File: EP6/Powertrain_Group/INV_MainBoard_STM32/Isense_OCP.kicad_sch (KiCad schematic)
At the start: 18 parts, among them J13 motorTemp, J5 current_DC, J6 to PhaseIsense, U15 LM2903

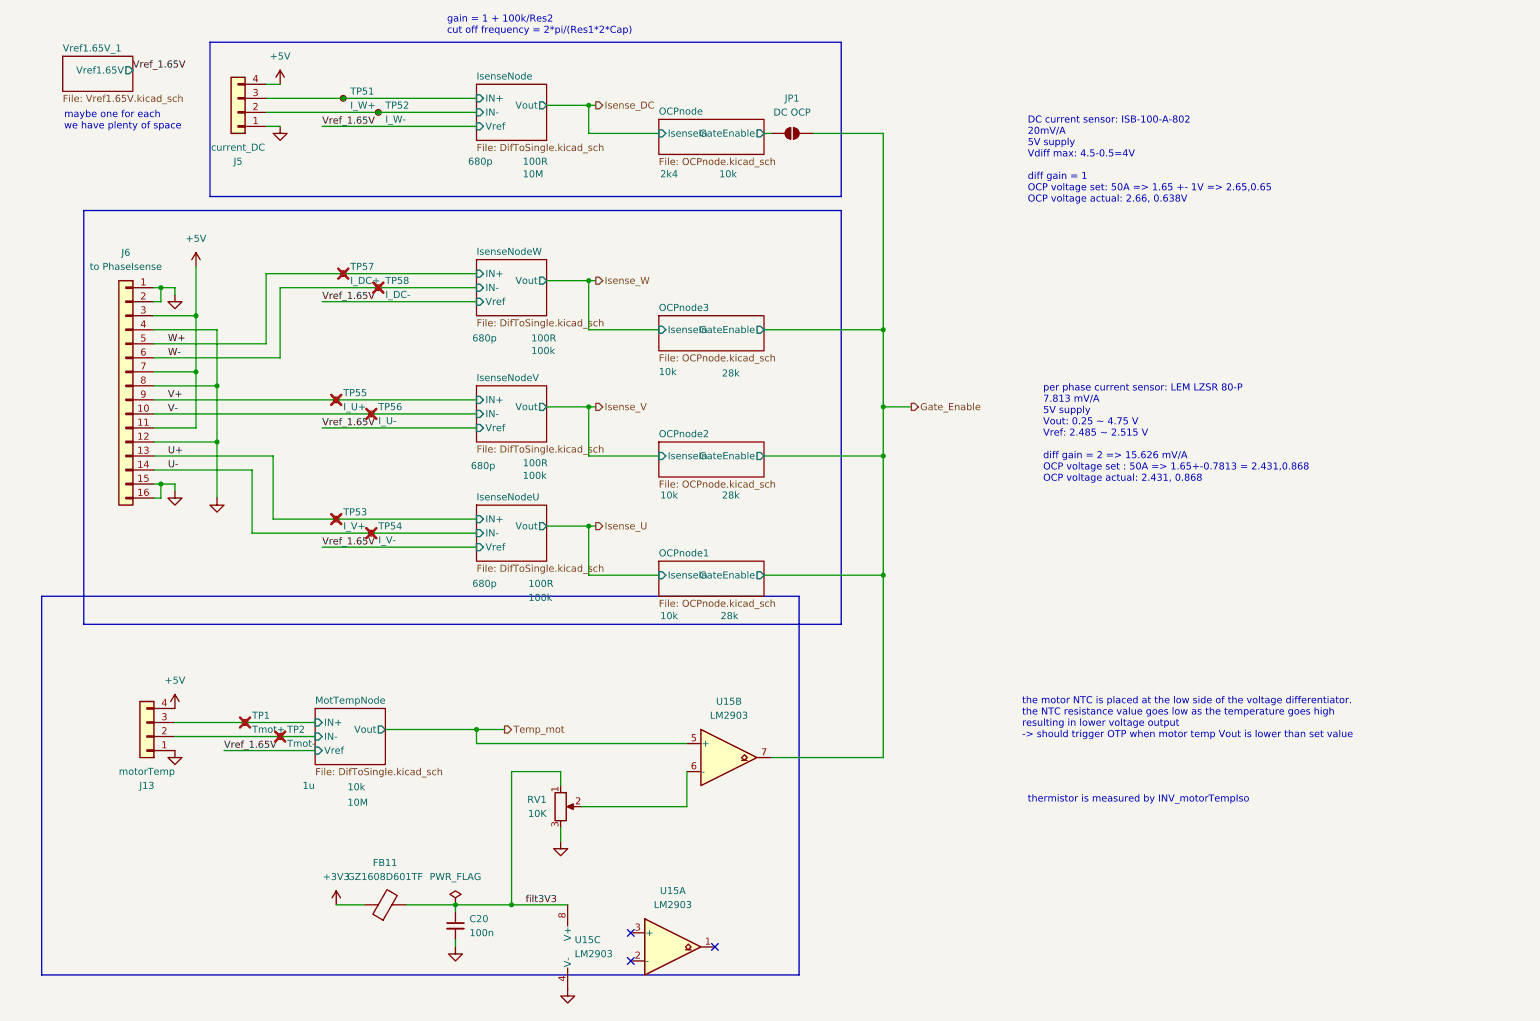
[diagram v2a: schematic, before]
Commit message: update INV_MainBoard_STM32 to V2.1
update for JLCPCB, include change in 1.65 Vref and some name change for easier JLCPCBA BOM selection
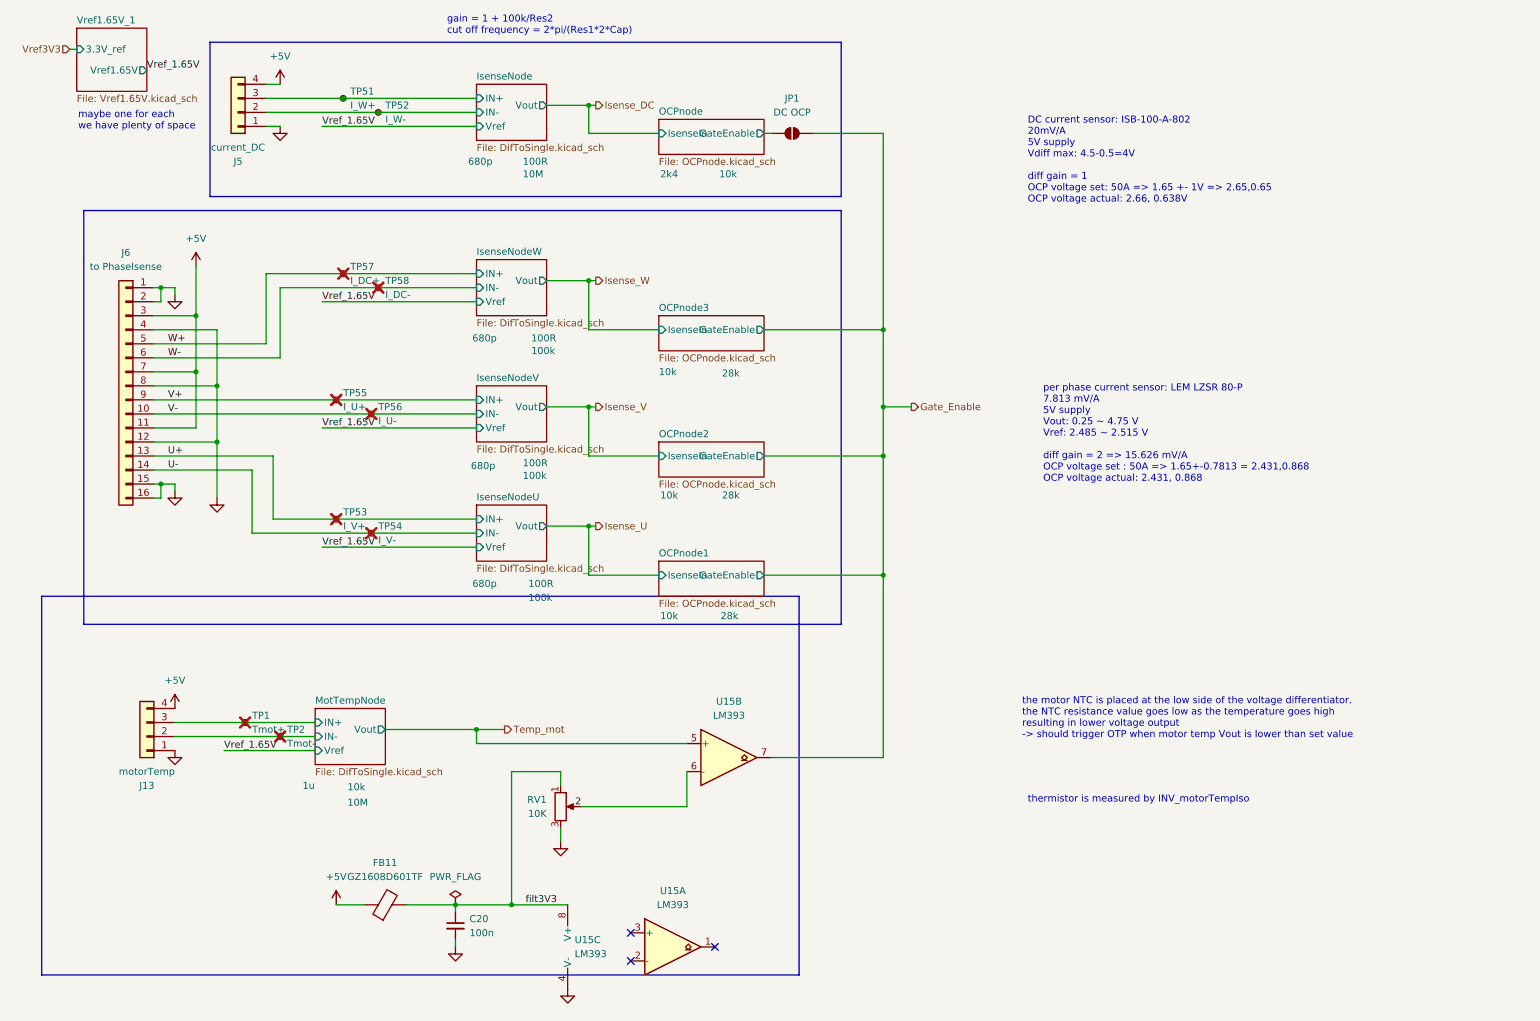
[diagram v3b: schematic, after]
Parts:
- U15: value LM2903 -> LM393; symbol Comparator:LM2903 -> Comparator:LM393
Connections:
- net +3V3 is gone; now on net +5V: FB11.1
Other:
- sheet Vref1.65V_1 ports: added 3.3V_ref; removed none
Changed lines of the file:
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@@
 	(title_block
 		(title "INV_MainBoard_STM32")
-		(rev "2.0")
+		(date "2025-02-28")
+		(rev "2.1")
 		(company "NTURacing Team")
 		(comment 1 "郭哲明 Jack Kuo")
@@
 	(wire
 		(pts
+			(xy 21.59 21.59) (xy 22.86 21.59)
+		)
+		(stroke
+			(width 0)
+			(type default)
+		)
+	)
+	(wire
+		(pts
 			(xy 156.21 36.83) (xy 168.91 36.83)
 		)
@@
 	(text "maybe one for each\nwe have plenty of space "
 		(exclude_from_sim no)
-		(at 20.574 36.322 0)
+		(at 23.114 36.322 0)
 		(effects
 			(font
@@
 	)
 	(label "Vref_1.65V"
-		(at 33.02 25.4 0)
+		(at 35.56 25.4 0)
 		(effects
 			(font
@@
 		)
 	)
+	(hierarchical_label "Vref3V3"
+		(shape input)
+		(at 21.59 21.59 180)
+		(effects
+			(font
+				(size 1.27 1.27)
+			)
+			(justify right)
+		)
+	)
 	(hierarchical_label "Isense_V"
 		(shape output)
@@
 	)
 	(symbol
-		(lib_id "Comparator:LM2903")
+		(lib_id "Comparator:LM393")
 		(at 140.97 149.86 0)
 		(unit 2)
@@
 			)
 		)
-		(property "Value" "LM2903"
+		(property "Value" "LM393"
 			(at 140.97 142.24 0)
 			(effects
@@
 			)
 		)
-		(property "Description" "Low-Power, Low-Offset Voltage, Dual Comparators, DIP-8/SOIC-8/SOP-8/TSSOP-8/VSSOP-8"
+		(property "Description" "Low-Power, Low-Offset Voltage, Dual Comparators, DIP-8/SOIC-8/TO-99-8"
 			(at 140.97 149.86 0)
 			(effects
@@
 	)
 	(symbol
-		(lib_id "power:+3V3")
-		(at 69.85 176.53 0)
-		(unit 1)
-		(exclude_from_sim no)
-		(in_bom yes)
-		(on_board yes)
-		(dnp no)
-		(fields_autoplaced yes)
-		(property "Reference" "#PWR093"
-			(at 69.85 180.34 0)
-			(effects
-				(font
-					(size 1.27 1.27)
-				)
-				(hide yes)
-			)
-		)
-		(property "Value" "+3V3"
-			(at 69.85 171.45 0)
-			(effects
-				(font
-					(size 1.27 1.27)
-				)
-			)
-		)
-		(property "Footprint" ""
-			(at 69.85 176.53 0)
-			(effects
-				(font
-					(size 1.27 1.27)
-				)
-				(hide yes)
-			)
-		)
-		(property "Datasheet" ""
-			(at 69.85 176.53 0)
-			(effects
-				(font
-					(size 1.27 1.27)
-				)
-				(hide yes)
-			)
-		)
-		(property "Description" "Power symbol creates a global label with name \"+3V3\""
-			(at 69.85 176.53 0)
-			(effects
-				(font
-					(size 1.27 1.27)
-				)
-				(hide yes)
-			)
-		)
-		(pin "1"
-		)
-		(instances
-			(project ""
-				(path "/963ad98e-e494-4953-a7e0-8b20a365a35d/a8cbfb17-6eb3-4a23-8b1d-6aae5b32a7fb"
-					(reference "#PWR093")
-					(unit 1)
-				)
-			)
-		)
-	)
-	(symbol
 		(lib_id "Jumper:SolderJumper_2_Open")
 		(at 152.4 36.83 0)
@@
 	)
 	(symbol
-		(lib_id "Comparator:LM2903")
+		(lib_id "Comparator:LM393")
 		(at 130.81 184.15 0)
 		(unit 1)
@@
 			)
 		)
-		(property "Value" "LM2903"
+		(property "Value" "LM393"
 			(at 130.81 176.53 0)
 			(effects
@@
 			)
 		)
-		(property "Description" "Low-Power, Low-Offset Voltage, Dual Comparators, DIP-8/SOIC-8/SOP-8/TSSOP-8/VSSOP-8"
+		(property "Description" "Low-Power, Low-Offset Voltage, Dual Comparators, DIP-8/SOIC-8/TO-99-8"
 			(at 130.81 184.15 0)
 			(effects
@@
 	)
 	(symbol
+		(lib_id "power:+5V")
+		(at 69.85 176.53 0)
+		(unit 1)
+		(exclude_from_sim no)
+		(in_bom yes)
+		(on_board yes)
+		(dnp no)
+		(fields_autoplaced yes)
+		(property "Reference" "#PWR093"
+			(at 69.85 180.34 0)
+			(effects
+				(font
+					(size 1.27 1.27)
+				)
+				(hide yes)
+			)
+		)
+		(property "Value" "+5V"
+			(at 69.85 171.45 0)
+			(effects
+				(font
+					(size 1.27 1.27)
+				)
+			)
+		)
+		(property "Footprint" ""
+			(at 69.85 176.53 0)
+			(effects
+				(font
+					(size 1.27 1.27)
+				)
+				(hide yes)
+			)
+		)
+		(property "Datasheet" ""
+			(at 69.85 176.53 0)
+			(effects
+				(font
+					(size 1.27 1.27)
+				)
+				(hide yes)
+			)
+		)
+		(property "Description" "Power symbol creates a global label with name \"+5V\""
+			(at 69.85 176.53 0)
+			(effects
+				(font
+					(size 1.27 1.27)
+				)
+				(hide yes)
+			)
+		)
+		(pin "1"
+		)
+		(instances
+			(project "INV_MainBoard_STM32"
+				(path "/963ad98e-e494-4953-a7e0-8b20a365a35d/a8cbfb17-6eb3-4a23-8b1d-6aae5b32a7fb"
+					(reference "#PWR093")
+					(unit 1)
+				)
+			)
+		)
+	)
+	(symbol
 		(lib_id "power:GND")
 		(at 40.64 101.6 0)
@@
 	)
 	(symbol
-		(lib_id "Comparator:LM2903")
+		(lib_id "Comparator:LM393")
 		(at 114.3 184.15 0)
 		(unit 3)
@@
 			)
 		)
-		(property "Value" "LM2903"
+		(property "Value" "LM393"
 			(at 113.03 185.42 0)
 			(effects
@@
 			)
 		)
-		(property "Description" "Low-Power, Low-Offset Voltage, Dual Comparators, DIP-8/SOIC-8/SOP-8/TSSOP-8/VSSOP-8"
+		(property "Description" "Low-Power, Low-Offset Voltage, Dual Comparators, DIP-8/SOIC-8/TO-99-8"
 			(at 114.3 184.15 0)
 			(effects
@@
 	)
 	(sheet
-		(at 20.32 22.86)
-		(size 12.7 6.35)
+		(at 22.86 17.78)
+		(size 12.7 11.43)
 		(fields_autoplaced yes)
 		(stroke
@@
 		)
 		(property "Sheetname" "Vref1.65V_1"
-			(at 20.32 22.1484 0)
+			(at 22.86 17.0684 0)
 			(effects
 				(font
@@
 		)
 		(property "Sheetfile" "Vref1.65V.kicad_sch"
-			(at 20.32 29.7946 0)
+			(at 22.86 29.7946 0)
 			(effects
 				(font
@@
 		)
 		(pin "Vref1.65V" output
-			(at 33.02 25.4 0)
+			(at 35.56 25.4 0)
 			(effects
 				(font
@@
 			)
 		)
+		(pin "3.3V_ref" input
+			(at 22.86 21.59 180)
+			(effects
+				(font
+					(size 1.27 1.27)
+				)
+				(justify left)
+			)
+		)

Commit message: update INV_MainBoard_STM32 to V3.0
PCB: INV_MainBoard_STM32 V3.0
V3.0 remove low volte trig
     add RC filt for OCP, OTP
     dedicated OTP, OCP pull down gate enable
     pending: fault hardware OTP/OCP latch
     pending: add QSPI DRAM
     use JST PH
     exterinal pull up for flt, ready
     fix CAN1, 2 label on board
     use 1k, 2k for encoder divider
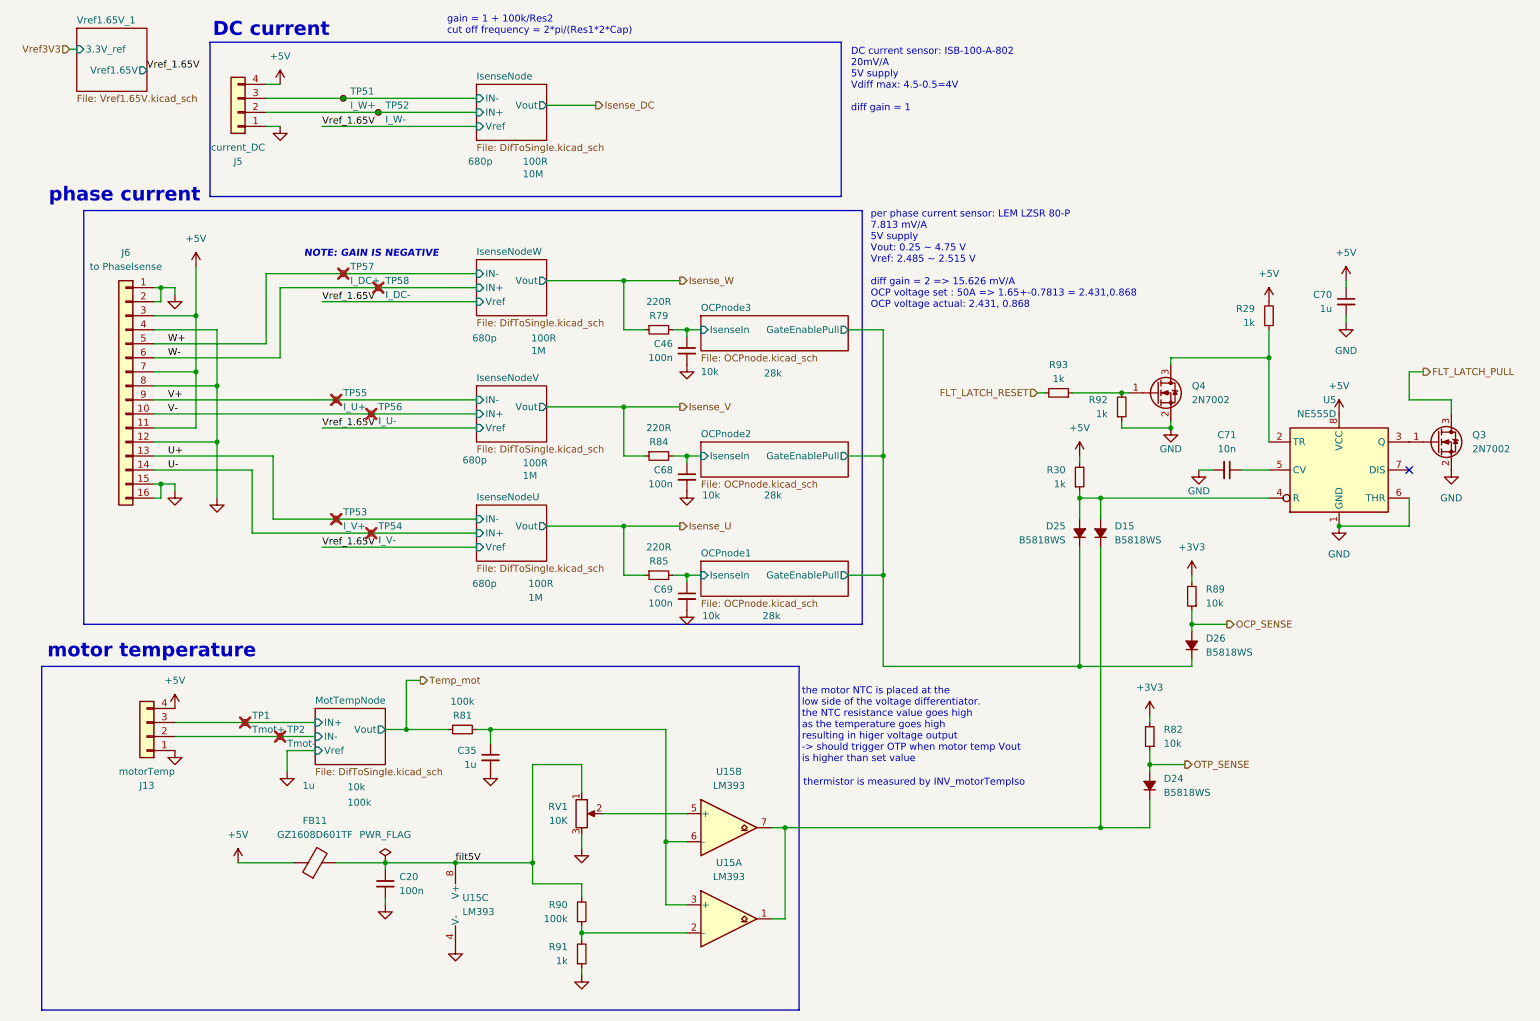
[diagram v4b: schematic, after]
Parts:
- removed JP1: DC OCP, Jumper:SolderJumper-2_P1.3mm_Open_RoundedPad1.0x1.5mm, symbol Jumper:SolderJumper_2_Open
- added C35, C70: 1u, Capacitor_SMD:C_0402_1005Metric, symbol Device:C_Small
- added C46, C68, C69: 100n, Capacitor_SMD:C_0402_1005Metric, symbol Device:C_Small
- added C71: 10n, Capacitor_SMD:C_0402_1005Metric, symbol Device:C_Small
- added D15, D24, D25, D26: B5818WS, Diode_SMD:D_SOD-323, symbol Device:D_Small_Filled
- added Q3, Q4: 2N7002, Package_TO_SOT_SMD:SOT-23, symbol Transistor_FET:2N7002
- added R29, R30, R91, R92, R93: 1k, Resistor_SMD:R_0402_1005Metric, symbol Device:R_Small
- added R79, R84, R85: 220R, Resistor_SMD:R_0402_1005Metric, symbol Device:R_Small
- added R81, R90: 100k, Resistor_SMD:R_0402_1005Metric, symbol Device:R_Small
- added R82, R89: 10k, Resistor_SMD:R_0402_1005Metric, symbol Device:R_Small
- added U5: NE555D, Package_SO:SOIC-8_3.9x4.9mm_P1.27mm, symbol Timer:NE555D
- J13, J5: footprint Connector_JST:JST_XH_B4B-XH-A_1x04_P2.50mm_Vertical -> Connector_JST:JST_PH_B4B-PH-K_1x04_P2.00mm_Vertical
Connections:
- net Gate_Enable is gone; now on an unnamed net: U15.7
- net +5V: now also C70.1, R29.2, R30.2, U5.8 (VCC)
- net GND: now also C35.2, C46.2, C68.2, C69.2, C70.2, C71.2, Q3.2 (S), Q4.2 (S), R91.1, R92.1, U5.1 (GND), U5.6 (THR)
- net IsenseNode/IN+: now also J5.2 (Pin_2), TP52.1; no longer J5.3 (Pin_3), TP51.1
- net IsenseNode/IN-: now also J5.3 (Pin_3), TP51.1; no longer J5.2 (Pin_2), TP52.1
- net Isense_U: now also R85.1
- net Isense_V: now also R84.1
- net Isense_W: now also R79.1
- net Temp_mot: now also R81.1; no longer U15.5 (+)
- net at RV1.2: now also U15.5 (+); no longer U15.6 (-)
- net at U15.1: now also D15.1 (K), D24.1 (K)
- net at U15.2 (-): now also R90.1, R91.2
- net at U15.3 (+): now also U15.6 (-), C35.1, R81.2
- net filt3V3 renamed filt5V
- net filt5V: now also R90.2
- new net: Q4.1 (G), R92.2, R93.1
- new net: Q3.1 (G), U5.3 (Q)
- new net: C71.1, U5.5 (CV)
- new net: Q4.3 (D), R29.1, U5.2 (TR)
- new net: D15.2 (A), D25.2 (A), R30.1, U5.4 (R)
- new net +3V3: R82.2, R89.2
- new net FLT_LATCH_PULL: Q3.3 (D)
- new net FLT_LATCH_RESET: R93.2
- new net OCP_SENSE: D26.2 (A), R89.1
- new net OCPnode1/GateEnablePull: D25.1 (K), D26.1 (K)
- new net OCPnode1/IsenseIn: C69.1, R85.2
- new net OCPnode2/IsenseIn: C68.1, R84.2
- new net OCPnode3/IsenseIn: C46.1, R79.2
- new net OTP_SENSE: D24.2 (A), R82.1
- no-connect marks 3 -> 1
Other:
- removed sheet OCPnode
- sheet OCPnode1 ports: added GateEnablePull; removed GateEnable
- sheet OCPnode2 ports: added GateEnablePull; removed GateEnable
- sheet OCPnode3 ports: added GateEnablePull; removed GateEnable
- note added: "DC current"
- note added: "DC current sensor: ISB-100-A-802 20mV/A 5V supply Vdiff max: 4.5-0.5=4V diff gain = 1"
- note added: "NOTE: GAIN IS NEGATIVE"
- note added: "motor temperature"
- note added: "phase current"
- note added: "the motor NTC is placed at the low side of the voltage differentiator. the NTC resistance value goes high as the temperature goes high resulting in higer voltage output -> should trigger OTP when motor temp Vout is higher than set value"
- note removed: "DC current sensor: ISB-100-A-802 20mV/A 5V supply Vdiff max: 4.5-0.5=4V diff gain = 1 OCP voltage set: 50A => 1.65 +- 1V => 2.65,0.65 OCP voltage actual: 2.66, 0.638V"
- note removed: "maybe one for each we have plenty of space"
- note removed: "the motor NTC is placed at the low side of the voltage differentiator. the NTC resistance value goes low as the temperature goes high resulting in lower voltage output -> should trigger OTP when motor temp Vout is lower than set value"
- moved on the sheet: C20, FB11, RV1, U15A, U15B, U15C
